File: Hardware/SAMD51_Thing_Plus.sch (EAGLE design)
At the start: 45 parts, among them J6 AMP FCI 10103594-0001LF, Q1 2.5A/30V, U1 MCP73831, U2 ATSAMD51J20A-A, U3 AP2112K-3.3V, U4 4MB Flash, Y1 32.768kHz

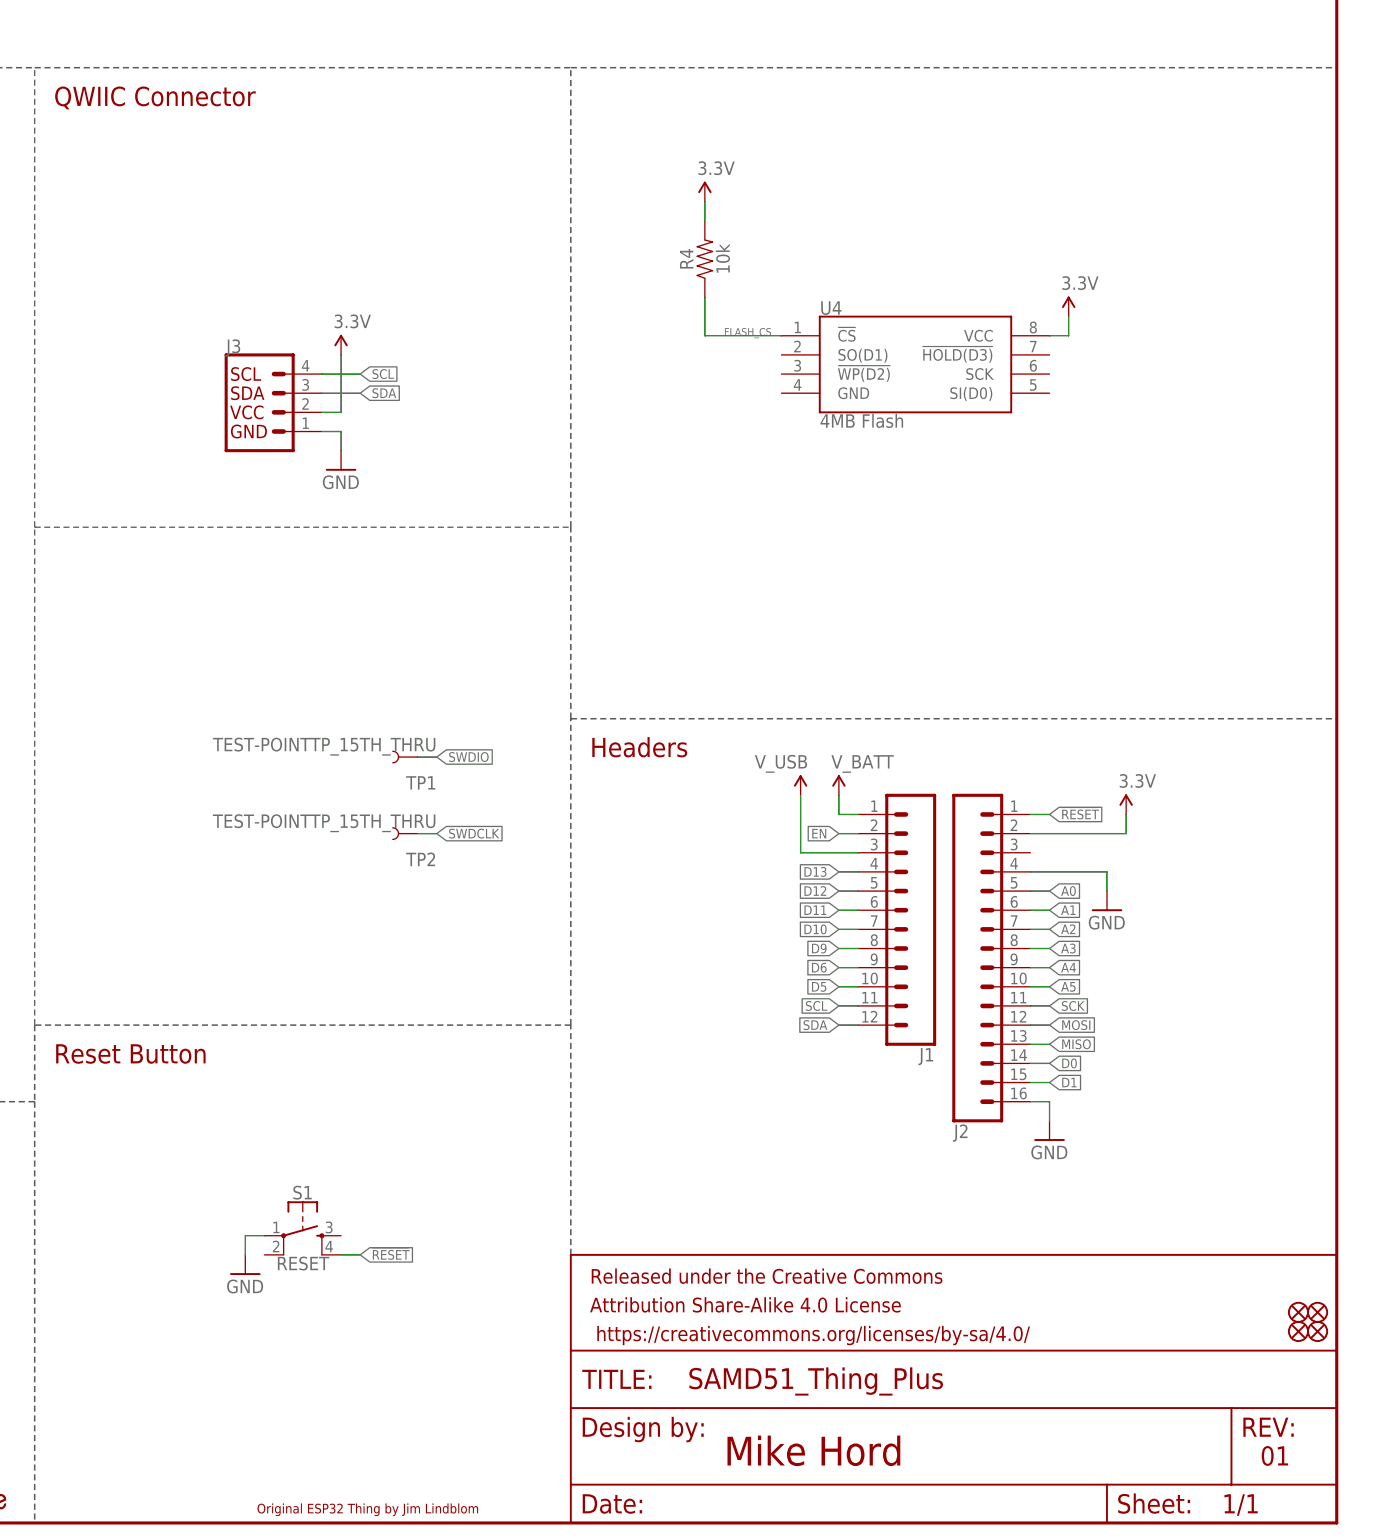
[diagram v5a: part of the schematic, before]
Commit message: Add flash, buzzard labels
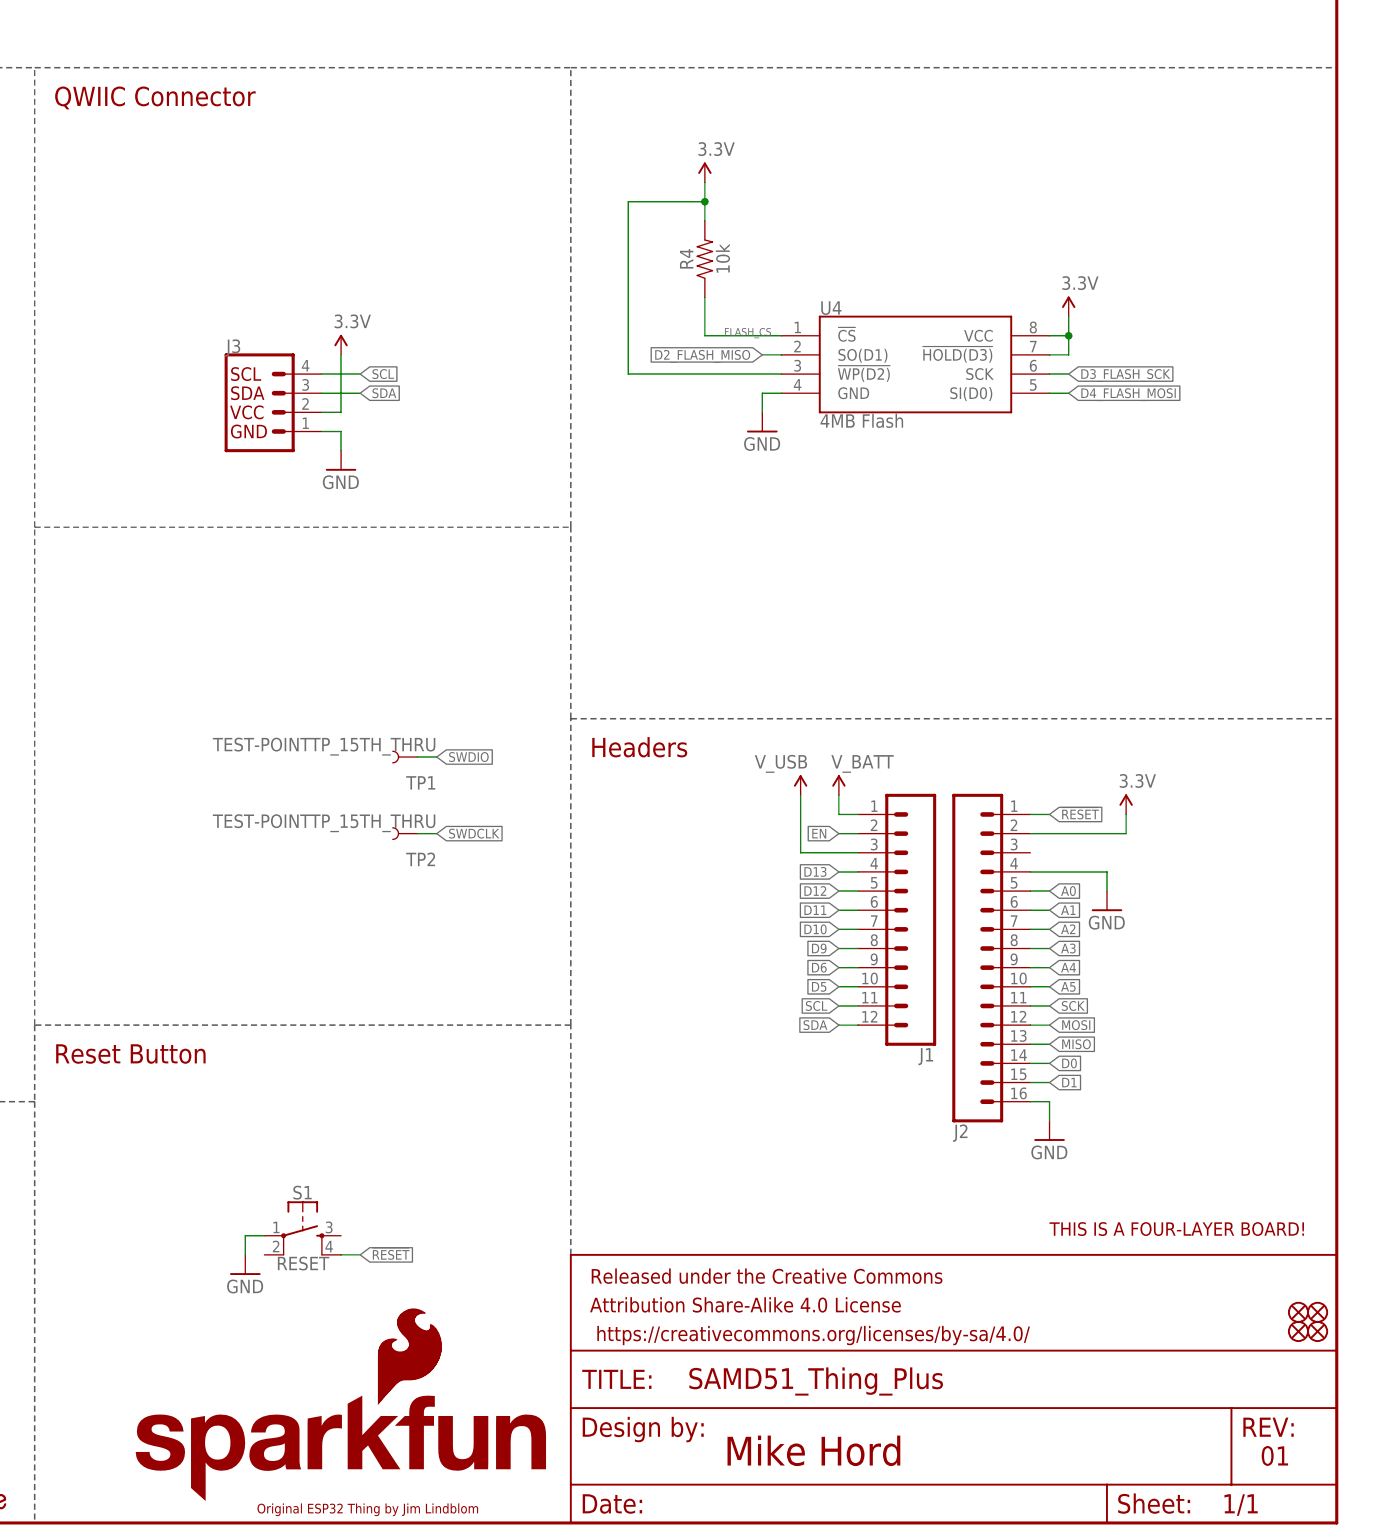
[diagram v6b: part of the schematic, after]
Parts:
- added LOGO1: FOUR_LAYER_WARNING, SparkFun-Aesthetics:FOUR_LAYER_WARNING
- added LOGO3: SFE_LOGO_NAME_FLAME.1_INCH, SparkFun-Aesthetics:SFE_LOGO_NAME_FLAME.1_INCH
- added LOGO4: SFE_LOGO_FLAME.1_INCH, SparkFun-Aesthetics:SFE_LOGO_FLAME.1_INCH
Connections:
- net 3.3V: now also U4.!HOLD(D3), U4.!WP(D2)
- net D2_FLASH_MISO: now also U4.SO(D1)
- net D3_FLASH_SCK: now also U4.SCK
- net D4_FLASH_MOSI: now also U4.SI(D0)
- net GND: now also U4.GND
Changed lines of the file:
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@@
 <part name="SUPPLY9" library="SparkFun-Aesthetics" deviceset="3.3V" device=""/>
 <part name="SUPPLY11" library="SparkFun-Aesthetics" deviceset="3.3V" device=""/>
+<part name="GND3" library="SparkFun-Aesthetics" deviceset="GND" device=""/>
+<part name="LOGO1" library="SparkFun-Aesthetics" deviceset="FOUR_LAYER_WARNING" device=""/>
+<part name="LOGO3" library="SparkFun-Aesthetics" deviceset="SFE_LOGO_NAME_FLAME" device=".1_INCH"/>
+<part name="LOGO4" library="SparkFun-Aesthetics" deviceset="SFE_LOGO_FLAME" device=".1_INCH"/>
 </parts>
 <sheets>
@@
 <instance part="U4" gate="G$1" x="373.38" y="152.4"/>
 <instance part="R4" gate="G$1" x="347.98" y="167.64" rot="R90"/>
-<instance part="SUPPLY9" gate="G$1" x="347.98" y="175.26"/>
+<instance part="SUPPLY9" gate="G$1" x="347.98" y="177.8"/>
 <instance part="SUPPLY11" gate="G$1" x="396.24" y="160.02"/>
+<instance part="GND3" gate="1" x="355.6" y="144.78"/>
+<instance part="LOGO1" gate="G$1" x="393.7" y="38.1"/>
+<instance part="LOGO3" gate="G$1" x="271.78" y="2.54"/>
+<instance part="LOGO4" gate="G$1" x="304.292" y="15.24"/>
 </instances>
 <busses>
@@
 <pinref part="SUPPLY9" gate="G$1" pin="3.3V"/>
 <wire x1="347.98" y1="172.72" x2="347.98" y2="175.26" width="0.1524" layer="91"/>
+<pinref part="U4" gate="G$1" pin="!WP(D2)"/>
+<wire x1="347.98" y1="175.26" x2="347.98" y2="177.8" width="0.1524" layer="91"/>
+<wire x1="358.14" y1="152.4" x2="337.82" y2="152.4" width="0.1524" layer="91"/>
+<wire x1="337.82" y1="152.4" x2="337.82" y2="175.26" width="0.1524" layer="91"/>
+<wire x1="337.82" y1="175.26" x2="347.98" y2="175.26" width="0.1524" layer="91"/>
+<junction x="347.98" y="175.26"/>
 </segment>
 <segment>
@@
 <pinref part="U4" gate="G$1" pin="VCC"/>
 <wire x1="396.24" y1="157.48" x2="393.7" y2="157.48" width="0.1524" layer="91"/>
+<pinref part="U4" gate="G$1" pin="!HOLD(D3)"/>
+<wire x1="393.7" y1="154.94" x2="396.24" y2="154.94" width="0.1524" layer="91"/>
+<wire x1="396.24" y1="154.94" x2="396.24" y2="157.48" width="0.1524" layer="91"/>
+<junction x="396.24" y="157.48"/>
 </segment>
 </net>
@@
 <pinref part="GND7" gate="1" pin="GND"/>
 </segment>
+<segment>
+<pinref part="GND3" gate="1" pin="GND"/>
+<wire x1="355.6" y1="147.32" x2="355.6" y2="149.86" width="0.1524" layer="91"/>
+<pinref part="U4" gate="G$1" pin="GND"/>
+<wire x1="355.6" y1="149.86" x2="358.14" y2="149.86" width="0.1524" layer="91"/>
+</segment>
 </net>
 <net name="D8" class="0">
@@
 <label x="91.44" y="121.92" size="1.27" layer="95" font="vector" rot="R180" xref="yes"/>
 </segment>
+<segment>
+<pinref part="U4" gate="G$1" pin="SCK"/>
+<wire x1="393.7" y1="152.4" x2="396.24" y2="152.4" width="0.1524" layer="91"/>
+<label x="396.24" y="152.4" size="1.27" layer="95" xref="yes"/>
+</segment>
 </net>
 <net name="D2_FLASH_MISO" class="0">
@@
 <wire x1="93.98" y1="109.22" x2="91.44" y2="109.22" width="0.1524" layer="91"/>
 <label x="91.44" y="109.22" size="1.27" layer="95" font="vector" rot="R180" xref="yes"/>
+</segment>
+<segment>
+<pinref part="U4" gate="G$1" pin="SO(D1)"/>
+<wire x1="358.14" y1="154.94" x2="355.6" y2="154.94" width="0.1524" layer="91"/>
+<label x="355.6" y="154.94" size="1.27" layer="95" rot="R180" xref="yes"/>
 </segment>
 </net>
@@
 <label x="91.44" y="124.46" size="1.27" layer="95" font="vector" rot="R180" xref="yes"/>
 </segment>
-</net>
+<segment>
+<pinref part="U4" gate="G$1" pin="SI(D0)"/>
+<wire x1="393.7" y1="149.86" x2="396.24" y2="149.86" width="0.1524" layer="91"/>
+<label x="396.24" y="149.86" size="1.27" layer="95" xref="yes"/>
+</segment>
+</net>

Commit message: Changes from review
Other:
- note removed: "Original ESP32 Thing by Jim Lindblom"
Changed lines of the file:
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@@
 <text x="332.74" y="104.14" size="2.54" layer="94" align="top-left">Headers</text>
 <text x="421.64" y="10.16" size="2.54" layer="94" font="vector" align="top-left">01</text>
-<text x="288.544" y="1.27" size="1.27" layer="94" font="vector" rot="MR180" align="top-left">Original ESP32 Thing by Jim Lindblom</text>
 <text x="69.088" y="17.78" size="0.4064" layer="94">C8 to be
 near U2.21</text>
